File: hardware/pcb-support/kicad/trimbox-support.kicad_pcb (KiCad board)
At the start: 2 copper layers, 23.4 x 29 mm, 19 parts, among them J1 RX / BEC, J2 GPS, U1 TPS563201, U2 LSM6DS3TR-C, U3 ESP32-S3 Mini Nano N16R8

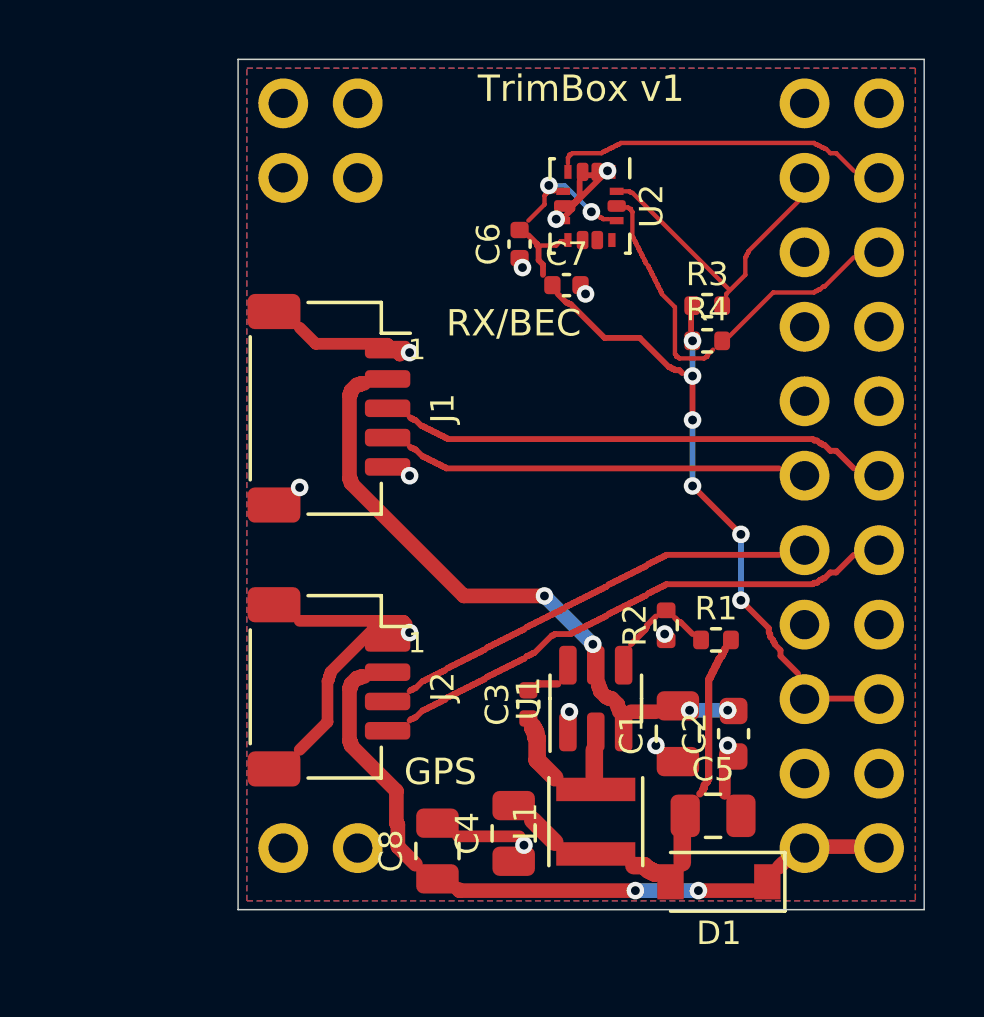
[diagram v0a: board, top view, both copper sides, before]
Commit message: PCB support : J1 remplacé par deux picots servo coudés (J1 TX, J3 RX)
- Deux picots coudés 2,54 mm 1×3 (S, +, −) au bord gauche : deux rallonges
  servo ordinaires depuis les sorties 2 (TX → IO16) et 3 (RX ← IO15) du
  récepteur ; le + amène le BEC. À souder soi-même (hors BOM JLCPCB).
- GPS (J2, JST SH 4) remonté en haut à gauche ; trous de tenue des rangées 1-2
  gauche retirés ; C8 près de J2 ; routage refait.
- Contrôle : aucune erreur (isolement 0,17 mm), réseaux continus, KiCad et
  Gerber revérifiés ; pastilles traversantes carrées dessinées en carré.
- Schéma, sérigraphie (S / - / TX / RX), notice et visualiseur 2D/3D à jour.

Co-Authored-By: Claude Opus 5.5 <noreply@anthropic.com>
Claude-Session: https://claude.ai/code/session_012Z8LmxLPqA1DRecvv9zmWy
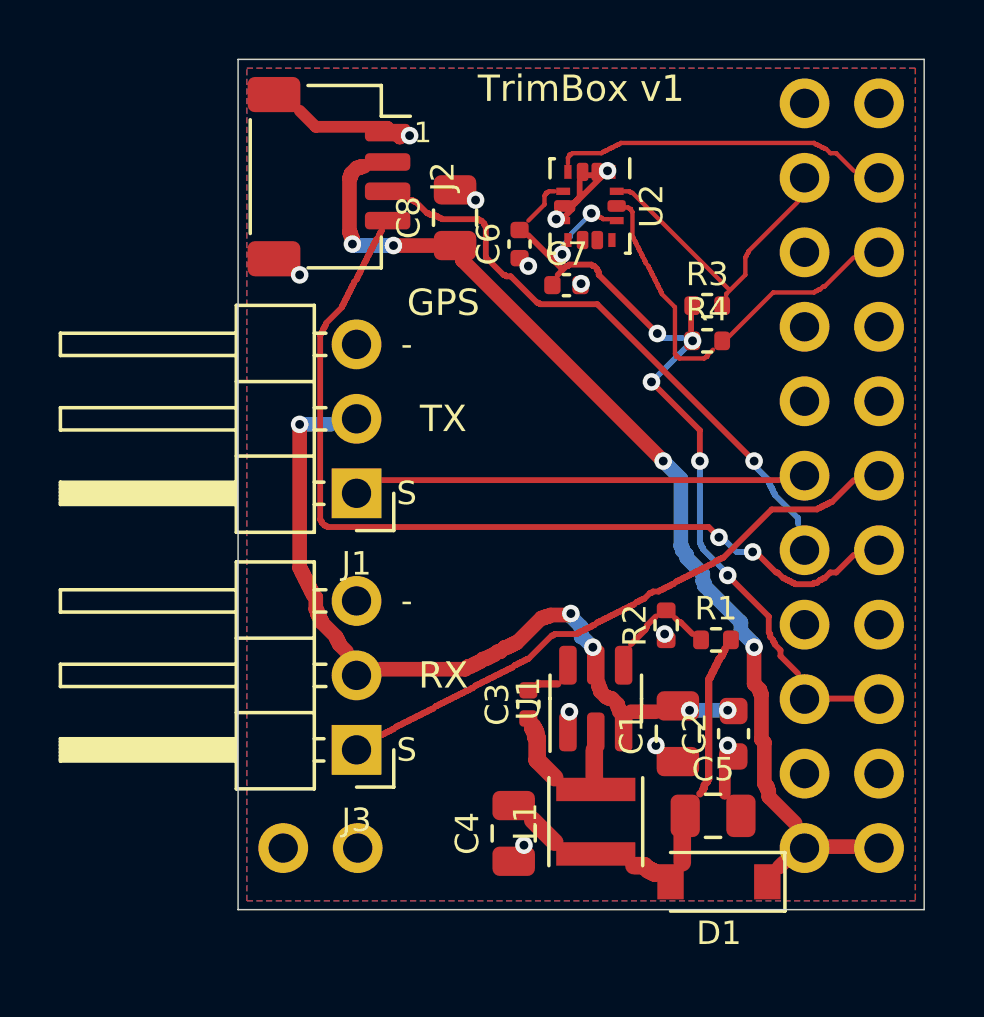
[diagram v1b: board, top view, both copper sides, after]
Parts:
- added R4: 4,7 kΩ, TrimBox:R_0402_1005Metric, F.Cu at (116.0, 73.2)
- C1: renamed from C2; value 100 nF 50 V -> 22 µF 25 V; footprint TrimBox:C_0603_1608Metric -> TrimBox:C_0805_2012Metric
- C2: renamed from C3; value 100 nF -> 100 nF 50 V; footprint TrimBox:C_0402_1005Metric -> TrimBox:C_0603_1608Metric
- C3: renamed from R1; value 56 kΩ 1 % -> 100 nF; footprint TrimBox:R_0402_1005Metric -> TrimBox:C_0402_1005Metric
- C5: renamed from D1; value B5819W -> 22 µF 25 V; footprint TrimBox:D_SOD-123 -> TrimBox:C_0805_2012Metric
- C7: renamed from R3; value 4,7 kΩ -> 100 nF; footprint TrimBox:R_0402_1005Metric -> TrimBox:C_0402_1005Metric
- C8: renamed from U2; value LSM6DS3TR-C -> 10 µF 25 V; footprint TrimBox:LGA-14_3x2.5mm_P0.5mm_LayoutBorder3x4y -> TrimBox:C_0805_2012Metric
- D1: renamed from C8; value 10 µF 25 V -> B5819W; footprint TrimBox:C_0805_2012Metric -> TrimBox:D_SOD-123
- J1: value RX / BEC -> Servo RX-TX; footprint TrimBox:JST_SH_SM05B-SRSS-TB_1x05-1MP_P1.00mm_Horizontal -> TrimBox:PinHeader_1x03_P2.54mm_Horizontal
- J2: renamed from U1; value TPS563201 -> GPS; footprint TrimBox:SOT-23-6 -> TrimBox:JST_SH_SM04B-SRSS-TB_1x04-1MP_P1.00mm_Horizontal
- J3: renamed from J2; value GPS -> Servo RX-RX; footprint TrimBox:JST_SH_SM04B-SRSS-TB_1x04-1MP_P1.00mm_Horizontal -> TrimBox:PinHeader_1x03_P2.54mm_Horizontal
- L1: renamed from C1; value 22 µF 25 V -> 3,3 µH; footprint TrimBox:C_0805_2012Metric -> TrimBox:L_Taiyo-Yuden_NR-30xx
- R1: renamed from R2; value 10 kΩ 1 % -> 56 kΩ 1 %
- R2: renamed from C4; value 22 µF 25 V -> 10 kΩ 1 %; footprint TrimBox:C_0805_2012Metric -> TrimBox:R_0402_1005Metric
- U1: renamed from L1; value 3,3 µH -> TPS563201; footprint TrimBox:L_Taiyo-Yuden_NR-30xx -> TrimBox:SOT-23-6
- U2: renamed from C6; value 100 nF -> LSM6DS3TR-C; footprint TrimBox:C_0402_1005Metric -> TrimBox:LGA-14_3x2.5mm_P0.5mm_LayoutBorder3x4y
- moved J2 20.0 mm to (103.1, 67.6), turned to 270 degrees
- moved D1 9.66 mm to (116.4, 91.7), turned to 180 degrees
- moved R2 8.80 mm to (114.6, 82.9)
- moved C2 7.07 mm to (116.9, 86.6)
- moved C4 6.83 mm to (109.4, 90.0), turned to 90 degrees
- moved C3 6.77 mm to (109.9, 85.6), turned to 90 degrees
- moved C7 4.85 mm to (111.2, 71.3)
- moved C8 4.62 mm to (107.4, 69.0), turned to 90 degrees
- moved U1 4.20 mm to (112.2, 85.4)
- moved L1 4.10 mm to (112.2, 89.6)
- moved J1 3.05 mm to (104.0, 78.4), turned to 180 degrees
- moved U2 2.73 mm to (112.0, 68.6), turned to 270 degrees
- moved J3 2.35 mm to (104.0, 87.2), turned to 180 degrees
- moved C5 2.26 mm to (116.2, 89.4), turned to 0 degrees
- moved C6 2.13 mm to (109.6, 69.9), turned to 90 degrees
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- renumbered C5 to C4, C7 to C6, R4 to R3
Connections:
- C2 pad 1: SW -> GND
- C2 pad 2: BST -> VBEC
- C3 pad 1: FB -> SW
- C3 pad 2: V5_BUCK -> BST
- C4 pad 1: V5_BUCK -> GND
- C4 pad 2: GND -> V5_BUCK
- C5 pad 1: +5V -> V5_BUCK
- C5 pad 2: V5_BUCK -> GND
- C6 pad 1: +3V3 -> GND
- C6 pad 2: GND -> +3V3
- C7 pad 2: SDA -> GND
- C8 pad 1: GND -> +5V
- D1 pad 2: GND -> V5_BUCK
- J1 pad 1: GND -> ELRS_TX
- J1 pad 3: ELRS_RX -> GND
- J2 pad 2: SW -> +5V
- J2 pad 3: VBEC -> GPS_TX
- J2 pad 4: FB -> GPS_RX
- J3 pad 1: GND -> ELRS_RX
- J3 pad 2: +5V -> VBEC
- J3 pad 3: GPS_TX -> GND
- L1 pad 1: GND -> V5_BUCK
- L1 pad 2: VBEC -> SW
- R1 pad 1: GND -> FB
- R1 pad 2: FB -> V5_BUCK
- R2 pad 2: V5_BUCK -> FB
- R3 pad 2: SCL -> SDA
- U1 pad 1: V5_BUCK -> GND
- U2 pad 2: +3V3 -> GND
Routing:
- net GPS_RX: track 17.5 -> 30.4 mm, vias 0 -> 2
- net +5V: track 18.8 -> 30.8 mm, vias 2 -> 4
- net GND: track 20.4 -> 8.51 mm, vias 13 -> 12
- net GPS_TX: track 14.5 -> 18.9 mm, vias 0 -> 1
- net VBEC: track 17.8 -> 21.7 mm, vias 4 -> 5
- net ELRS_RX: track 15.9 -> 19.8 mm
- net +3V3: track 26.2 -> 27.1 mm, vias 8 -> 7
- net ELRS_TX: track 12.9 -> 13.6 mm
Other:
- board text added: "-"
- board text added: "RX"
- board text added: "S"
- board text added: "TX"
- board text removed: "RX/BEC"

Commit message: PCB support : pastilles à souder pour les fils du récepteur (plus rien ne dépasse)
- J1 : 4 pastilles traversantes (trou 1,1 mm, pas 3 mm) TX, RX, +, − au
  bord gauche, à la place des picots coudés (J3 supprimé) : fils de deux
  rallonges servo coupées, aucune excroissance hors du contour.
- Routage refait ; contrôle : aucune erreur (isolement 0,177 mm), réseaux
  continus, KiCad et Gerber revérifiés.
- Schéma, sérigraphie, notice et visualiseur 2D/3D à jour.

Co-Authored-By: Claude Opus 5.5 <noreply@anthropic.com>
Claude-Session: https://claude.ai/code/session_012Z8LmxLPqA1DRecvv9zmWy
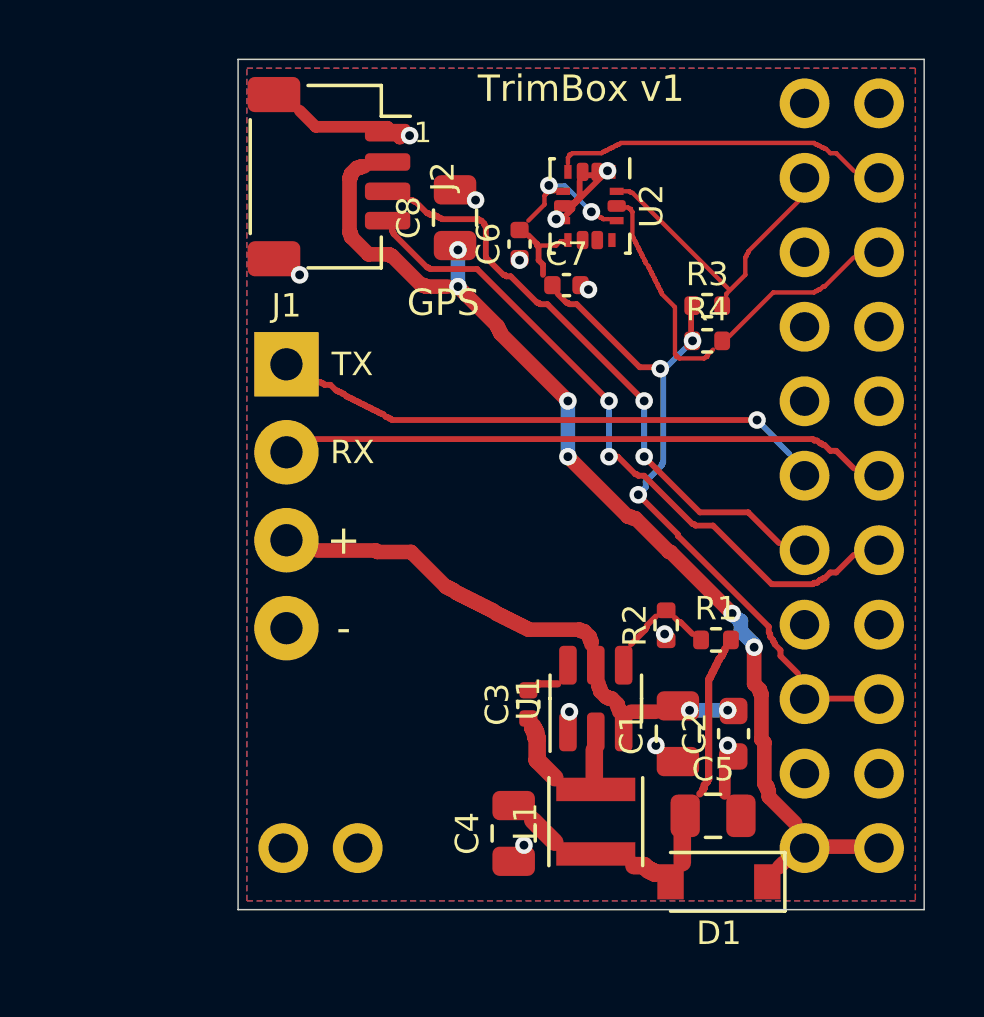
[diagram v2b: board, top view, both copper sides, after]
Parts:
- removed the R4 at (116.0, 73.2)
- C1: renamed from L1; value 3,3 µH -> 22 µF 25 V; footprint TrimBox:L_Taiyo-Yuden_NR-30xx -> TrimBox:C_0805_2012Metric
- C2: renamed from C1; value 22 µF 25 V -> 100 nF 50 V; footprint TrimBox:C_0805_2012Metric -> TrimBox:C_0603_1608Metric
- C3: renamed from C2; value 100 nF 50 V -> 100 nF; footprint TrimBox:C_0603_1608Metric -> TrimBox:C_0402_1005Metric
- C4: renamed from R2; value 10 kΩ 1 % -> 22 µF 25 V; footprint TrimBox:R_0402_1005Metric -> TrimBox:C_0805_2012Metric
- C6: renamed from U2; value LSM6DS3TR-C -> 100 nF; footprint TrimBox:LGA-14_3x2.5mm_P0.5mm_LayoutBorder3x4y -> TrimBox:C_0402_1005Metric
- C8: renamed from D1; value B5819W -> 10 µF 25 V; footprint TrimBox:D_SOD-123 -> TrimBox:C_0805_2012Metric
- D1: renamed from C5; value 22 µF 25 V -> B5819W; footprint TrimBox:C_0805_2012Metric -> TrimBox:D_SOD-123
- J1: value Servo RX-TX -> Fils récepteur; footprint TrimBox:PinHeader_1x03_P2.54mm_Horizontal -> TrimBox:TrimBox_Pastilles_fils_4x1.1mm
- J2: renamed from J3; value Servo RX-RX -> GPS; footprint TrimBox:PinHeader_1x03_P2.54mm_Horizontal -> TrimBox:JST_SH_SM04B-SRSS-TB_1x04-1MP_P1.00mm_Horizontal
- L1: renamed from U1; value TPS563201 -> 3,3 µH; footprint TrimBox:SOT-23-6 -> TrimBox:L_Taiyo-Yuden_NR-30xx
- R1: renamed from C3; value 100 nF -> 56 kΩ 1 %; footprint TrimBox:C_0402_1005Metric -> TrimBox:R_0402_1005Metric
- R2: renamed from R1; value 56 kΩ 1 % -> 10 kΩ 1 %
- R3: renamed from C7; value 100 nF -> 4,7 kΩ; footprint TrimBox:C_0402_1005Metric -> TrimBox:R_0402_1005Metric
- U1: renamed from J2; value GPS -> TPS563201; footprint TrimBox:JST_SH_SM04B-SRSS-TB_1x04-1MP_P1.00mm_Horizontal -> TrimBox:SOT-23-6
- U2: renamed from C8; value 10 µF 25 V -> LSM6DS3TR-C; footprint TrimBox:C_0805_2012Metric -> TrimBox:LGA-14_3x2.5mm_P0.5mm_LayoutBorder3x4y
- moved C8 24.4 mm to (107.4, 69.0), turned to 90 degrees
- moved U1 20.0 mm to (112.2, 85.4), turned to 90 degrees
- moved J2 19.6 mm to (103.1, 67.6), turned to 270 degrees
- moved C4 8.80 mm to (109.4, 90.0)
- moved C3 7.07 mm to (109.9, 85.6)
- moved C5 6.83 mm to (116.2, 89.4), turned to 0 degrees
- moved R1 6.77 mm to (116.3, 83.4), turned to 0 degrees
- moved J1 5.01 mm to (101.7, 74.0), turned to 0 degrees
- moved R3 4.85 mm to (116.0, 72.0)
- moved U2 4.62 mm to (112.0, 68.6), turned to 270 degrees
- moved L1 4.20 mm to (112.2, 89.6)
- moved C1 4.10 mm to (115.0, 86.6)
- moved C6 2.73 mm to (109.6, 69.9), turned to 90 degrees
- moved D1 2.26 mm to (116.4, 91.7), turned to 180 degrees
- moved C7 2.13 mm to (111.2, 71.3), turned to 0 degrees
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- renumbered C4 to C5, C6 to C7, R3 to R4
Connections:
- C1 pad 1: V5_BUCK -> GND
- C1 pad 2: SW -> VBEC
- C3 pad 1: GND -> SW
- C3 pad 2: VBEC -> BST
- C4 pad 2: FB -> V5_BUCK
- C5 pad 1: GND -> V5_BUCK
- C5 pad 2: V5_BUCK -> GND
- C6 pad 2: GND -> +3V3
- C7 pad 1: GND -> +3V3
- C7 pad 2: +3V3 -> GND
- C8 pad 2: V5_BUCK -> GND
- D1 pad 1: V5_BUCK -> +5V
- D1 pad 2: GND -> V5_BUCK
- J1 pad 2: VBEC -> ELRS_RX
- J1 pad 3: GND -> VBEC
- J2 pad 1: ELRS_RX -> GND
- J2 pad 2: VBEC -> +5V
- J2 pad 3: GND -> GPS_TX
- L1 pad 1: GND -> V5_BUCK
- R1 pad 1: SW -> FB
- R1 pad 2: BST -> V5_BUCK
- R2 pad 1: FB -> GND
- R2 pad 2: V5_BUCK -> FB
- R3 pad 2: GND -> SDA
- R4 pad 2: SDA -> SCL
- U1 pad 2: +5V -> SW
- U1 pad 3: GPS_TX -> VBEC
- U1 pad 4: GPS_RX -> FB
- U2 pad 1: +5V -> GND
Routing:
- net GPS_RX: track 30.4 -> 22.3 mm
- net VBEC: track 21.7 -> 14.3 mm, vias 5 -> 2
- net ELRS_TX: track 13.6 -> 17.1 mm, vias 0 -> 1
- net +5V: track 30.8 -> 32.3 mm, vias 4 -> 6
- net ELRS_RX: track 19.8 -> 18.8 mm
- net GPS_TX: track 18.9 -> 19.2 mm, vias 1 -> 2
- net +3V3: track 27.1 -> 26.9 mm, vias 7 -> 5
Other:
- board text added: "+"
- board text removed: "S"

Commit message: PCB support : 2 picots de tenue en haut à gauche, connexions décalées vers le bas
- Trous de tenue rangée 1 gauche (IO3, IO1) rétablis : l'ESP32 est tenue
  aux deux bouts du côté gauche (rangées 1 et 11) et sur toute la droite.
- Connecteur GPS J2 et pastilles J1 descendus ; C8 suit J2 ; routage refait.
- Contrôle : aucune erreur, réseaux continus, KiCad et Gerber revérifiés.

Co-Authored-By: Claude Opus 5.5 <noreply@anthropic.com>
Claude-Session: https://claude.ai/code/session_012Z8LmxLPqA1DRecvv9zmWy
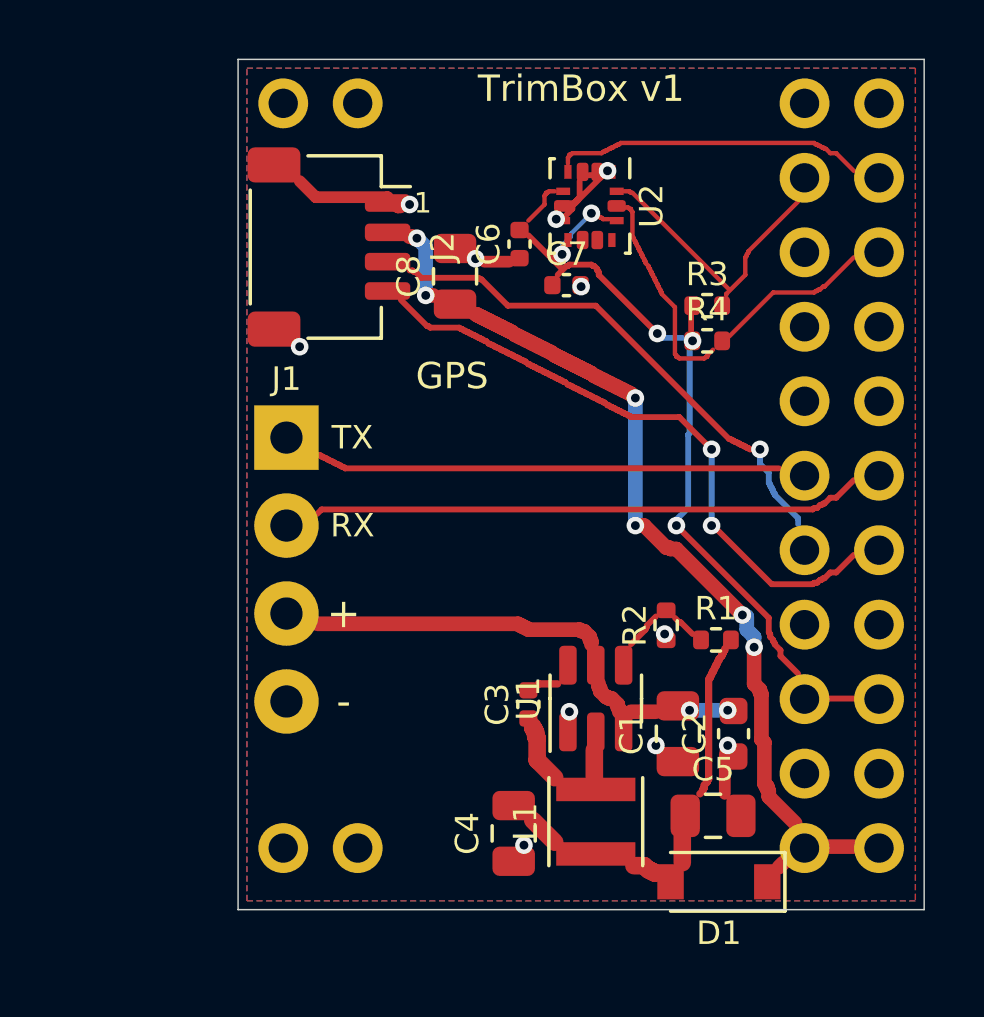
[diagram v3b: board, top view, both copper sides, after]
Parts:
- moved J1 2.50 mm to (101.7, 76.5)
- moved J2 2.40 mm to (103.1, 70.0)
- moved C8 2.00 mm to (107.4, 71.0)
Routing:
- net +5V: track 32.3 -> 27.5 mm
- net GPS_TX: track 19.2 -> 17.6 mm, vias 2 -> 1
- net ELRS_TX: track 17.1 -> 15.9 mm, vias 1 -> 0
- net VBEC: track 14.3 -> 13.2 mm
- net GPS_RX: track 22.3 -> 21.4 mm
- net GND: track 8.51 -> 9.34 mm, vias 12 -> 11
